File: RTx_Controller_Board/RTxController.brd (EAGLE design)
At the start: 161.3 x 90.2 mm, 197 parts, among them IC2 MAX5984C, J22 Debug Header, SW1 COM08720, U1 STM32F407ZXT, U2 TPD4S012, U3 KSZ8081, X4 MINI-USB-32005-301, X8 0826-1X1T-GJ-F

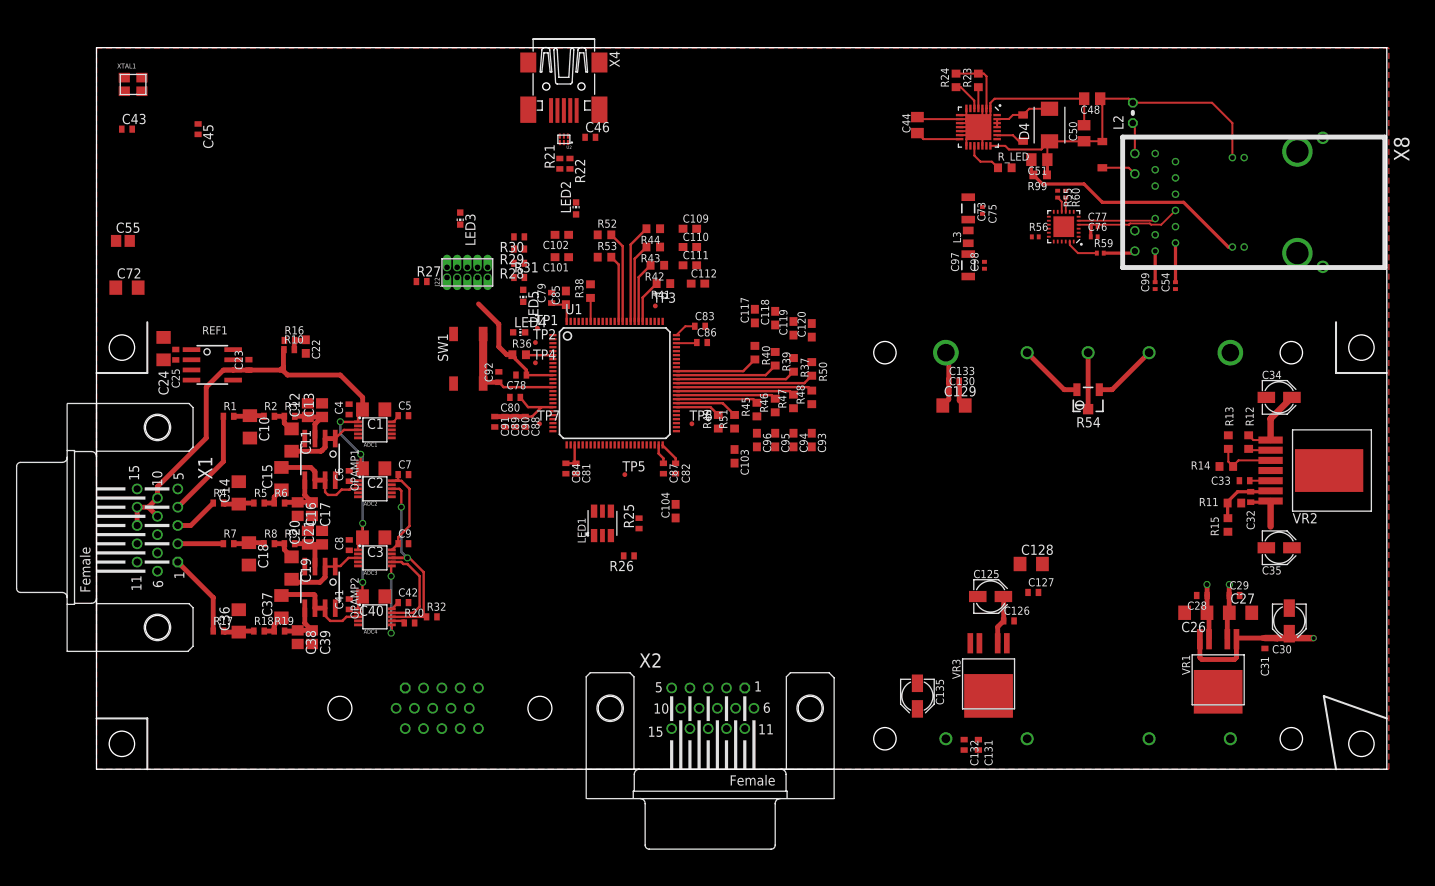
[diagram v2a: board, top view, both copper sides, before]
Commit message: Rtx Controller board updated, all that remains are power planes and rework by Rob. Initial check in of crystal.lbr.
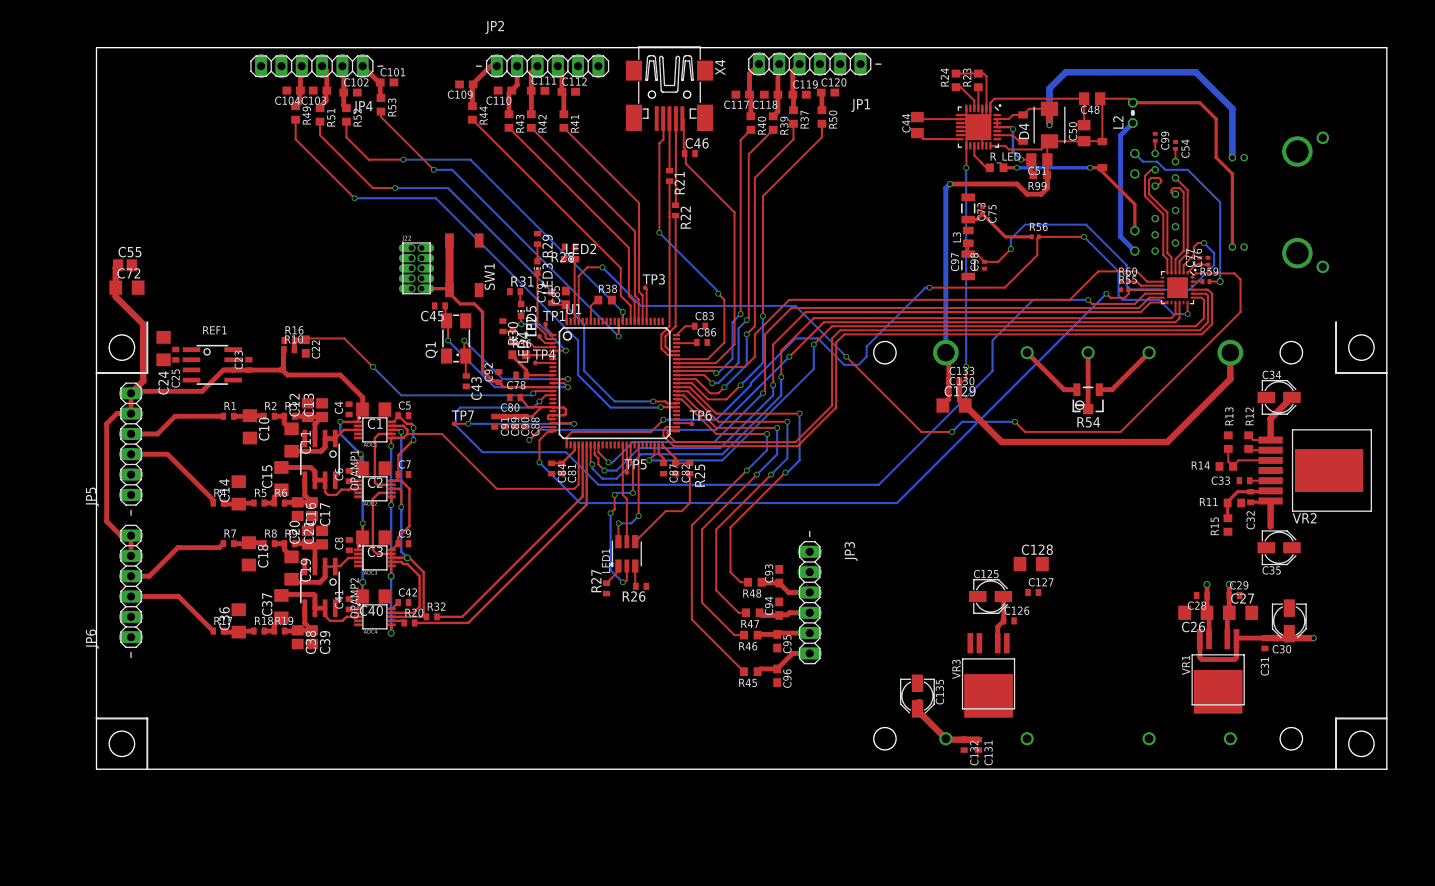
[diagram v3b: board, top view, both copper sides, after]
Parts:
- removed U2: TPD4S012, rtx:TPD4S012
- removed X1, X2, X3: (no value), con-subd:HDF15H
- removed XTAL1: ABM8G, motorFeedback:ABM8G
- added JP1, JP2, JP3, JP4, JP5, JP6: (no value), pinhead:1X06
- added Q1: (no value), crystal:CTS406
- moved C104 71.0 mm to (24.6, 84.8), turned to 180 degrees
- moved C103 69.1 mm to (27.9, 84.8), turned to 180 degrees
- moved R49 65.4 mm to (24.9, 82.0), turned to 270 degrees
- moved R51 64.5 mm to (27.9, 81.8), turned to 270 degrees
- moved C43 52.8 mm to (46.2, 48.5), turned to 270 degrees
- moved R27 44.8 mm to (63.8, 22.6), turned to 90 degrees
- moved C45 37.4 mm to (42.9, 57.9), turned to 180 degrees
- moved R52 35.6 mm to (31.2, 81.8), turned to 270 degrees
- moved R53 33.8 mm to (35.6, 83.1), turned to 270 degrees
- moved C109 33.3 mm to (46.2, 85.6), turned to 180 degrees
- moved R45 32.8 mm to (81.8, 12.2), turned to 180 degrees
- moved C102 31.8 mm to (31.8, 84.6), turned to 0 degrees
- moved R50 31.5 mm to (90.7, 81.5)
- moved R37 31.0 mm to (87.1, 81.5)
- moved C101 30.9 mm to (36.3, 85.9), turned to 0 degrees
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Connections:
- removed net SPI_NSS: ADC1.6, ADC1.9, ADC2.6, ADC3.6, ADC4.6
- net +5.000VREF: now also JP5.5, JP5.6, JP6.5, JP6.6; no longer X1.10, X1.13, X1.14, X1.9
- net ADC_CNV: now also ADC1.6, ADC1.9, ADC2.6, ADC3.6, ADC4.6
- net D+: no longer U2.1
- net D-: no longer U2.2
- net GND: now also JP1.1, JP1.2, JP2.5, JP2.6, JP3.1, JP3.2, JP4.5, JP4.6, JP5.1, JP5.2, JP6.1, JP6.2; no longer U2.4, X1.5, X1.6, X1.7, X1.8, X2.10, X2.5, X2.6, X2.7, X2.8, X3.10, X3.5, X3.6, X3.7, X3.8
- net N$14: now also JP6.4; no longer X1.2
- net N$42: now also JP3.6; no longer X2.15
- net N$45: now also JP3.5; no longer X2.14
- net N$46: now also JP3.4; no longer X2.13
- net N$47: now also JP3.3; no longer X2.12
- net N$48: now also JP4.4; no longer X2.4
- net N$49: now also JP4.3; no longer X2.3
- net N$50: now also JP4.2; no longer X2.2
- net N$51: now also JP4.1; no longer X2.1
- net N$52: now also JP2.4; no longer X3.4
- net N$53: now also JP2.3; no longer X3.3
- net N$54: now also JP2.2; no longer X3.2
- net N$55: now also JP2.1; no longer X3.1
- net N$6: now also JP5.4; no longer X1.4
- net N$61: now also JP1.3; no longer X3.15
- net N$62: now also JP1.4; no longer X3.14
- net N$63: now also JP1.5; no longer X3.13
- net N$64: now also JP1.6; no longer X3.12
- net N$7: now also JP6.3; no longer X1.1
- net N$9: now also JP5.3; no longer X1.3
- net OSC_IN: now also Q1.1; no longer XTAL1.1
- net OSC_OUT: now also Q1.3; no longer XTAL1.3
- net REF_MONITOR: now also U1.15; no longer U1.37
- net USB_ID: no longer U2.3
- net USB_VBUS: no longer U2.6
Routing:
- net ETH_MDC: track 0.00 -> 118.6 mm, vias 0 -> 2
- net EPHY_NRST: track 0.00 -> 115.3 mm, vias 0 -> 4
- net ETH_MDINT: track 0.00 -> 101.1 mm, vias 0 -> 4
- net ETH_MDIO: track 1.99 -> 96.8 mm, vias 0 -> 2
- net ETH_RMII_REF_CLK: track 0.00 -> 93.2 mm, vias 0 -> 2
- net ETH_CRS_DV: track 0.00 -> 89.7 mm, vias 0 -> 2
- net ETH_TXD1: track 0.00 -> 89.2 mm
- net ETH_RXD0: track 0.00 -> 86.5 mm, vias 0 -> 2
- net ETH_TXD0: track 0.00 -> 85.9 mm
- net ETH_RXD1: track 0.00 -> 84.7 mm, vias 0 -> 2
- net ETH_TX_EN: track 0.00 -> 84.5 mm, vias 0 -> 2
- net POE-: track 65.8 -> 137.7 mm, vias 0 -> 2
- net MCO1-ETH-CLK: track 0.00 -> 67.9 mm
- net ADC_CNV: track 0.00 -> 62.2 mm, vias 0 -> 4
- net WATCHDOG_LAT_OUT: track 5.64 -> 66.5 mm, vias 0 -> 2
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- removed copper zone on layer 1, net GND

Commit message: Repositioned LDO's created power planes.
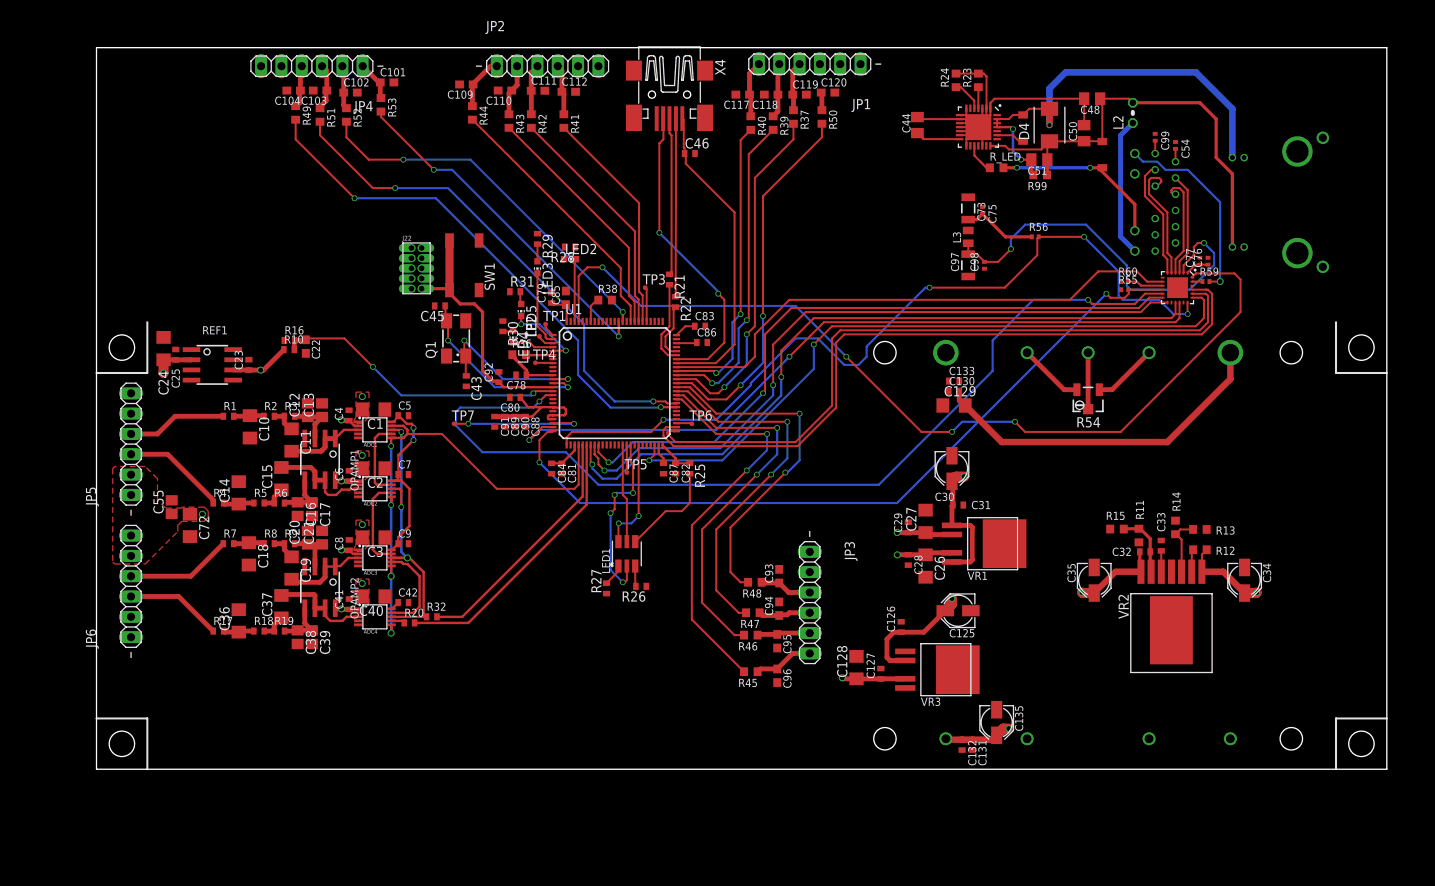
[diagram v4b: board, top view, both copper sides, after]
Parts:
- moved C30 46.3 mm to (106.9, 37.6)
- moved C31 42.1 mm to (107.7, 33.0), turned to 0 degrees
- moved C29 41.6 mm to (101.5, 30.2), turned to 90 degrees
- moved C27 41.0 mm to (103.6, 31.0), turned to 90 degrees
- moved C28 37.0 mm to (101.5, 26.2), turned to 270 degrees
- moved C26 34.3 mm to (103.6, 25.4), turned to 270 degrees
- moved VR1 32.9 mm to (112.0, 28.2), turned to 270 degrees
- moved C55 30.8 mm to (9.40, 32.8), turned to 90 degrees
- moved C72 30.7 mm to (11.7, 30.5), turned to 270 degrees
- moved VR2 28.6 mm to (134.4, 17.0), turned to 180 degrees
- moved C128 25.4 mm to (95.0, 12.7), turned to 90 degrees
- moved C35 23.5 mm to (124.7, 23.6), turned to 270 degrees
- moved C34 23.3 mm to (143.5, 23.6), turned to 270 degrees
- moved C127 21.6 mm to (98.0, 11.9), turned to 90 degrees
- moved C32 14.9 mm to (131.1, 27.2), turned to 180 degrees
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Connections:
- removed net VIO: ADC1.10, ADC2.10, ADC3.10, C5.1, C7.1, C9.1
- removed net VIO@10: ADC4.10, C42.1
- net +3.3V: now also ADC1.10, ADC2.10, ADC3.10, ADC4.10, C42.1, C5.1, C7.1, C9.1
- net +5.000VREF: now also JP5.1, JP5.2; no longer JP5.5, JP5.6
- net GND: now also JP5.5, JP5.6; no longer JP5.1, JP5.2
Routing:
- net +5.000VREF: track 112.6 -> 7.51 mm, vias 4 -> 6
- net POE+: track 99.9 -> 56.8 mm, vias 1 -> 0
- net POE-: track 137.7 -> 106.1 mm, vias 2 -> 0
- net +3.3V: track 55.5 -> 79.3 mm, vias 1 -> 3
- net VIO: track 22.7 -> 0.00 mm, vias 2 -> 0
- net D-: track 6.51 -> 19.7 mm
- net +8V: track 0.00 -> 13.1 mm, vias 0 -> 2
- net USB_D-: track 23.6 -> 10.6 mm
- net USB_D+: track 18.5 -> 7.07 mm
- net D+: track 10.8 -> 22.3 mm
- net +5V: track 7.19 -> 18.0 mm, vias 1 -> 5
- net +12V: track 33.2 -> 43.4 mm, vias 1 -> 3
- net VIO@10: track 1.13 -> 0.00 mm
- net +9-36V: track 20.4 -> 19.5 mm, vias 0 -> 2
- added copper zone on layer 3, net +12V
- added copper zone on layer 3, net +3.3V
- added copper zone on layer 1, net +5.000VREF
- added copper zone on layer 3, net +5.000VREF
- added copper zone on layer 3, net +5V
- added copper zone on layer 3, net +8V
- added copper zone on layer 3, net +9-36V
- added copper zone on layer 3, net POE+
- added copper zone on layer 3, net POE-

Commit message: Added termination resistors to RMII bus, adjusted width of digital signals.
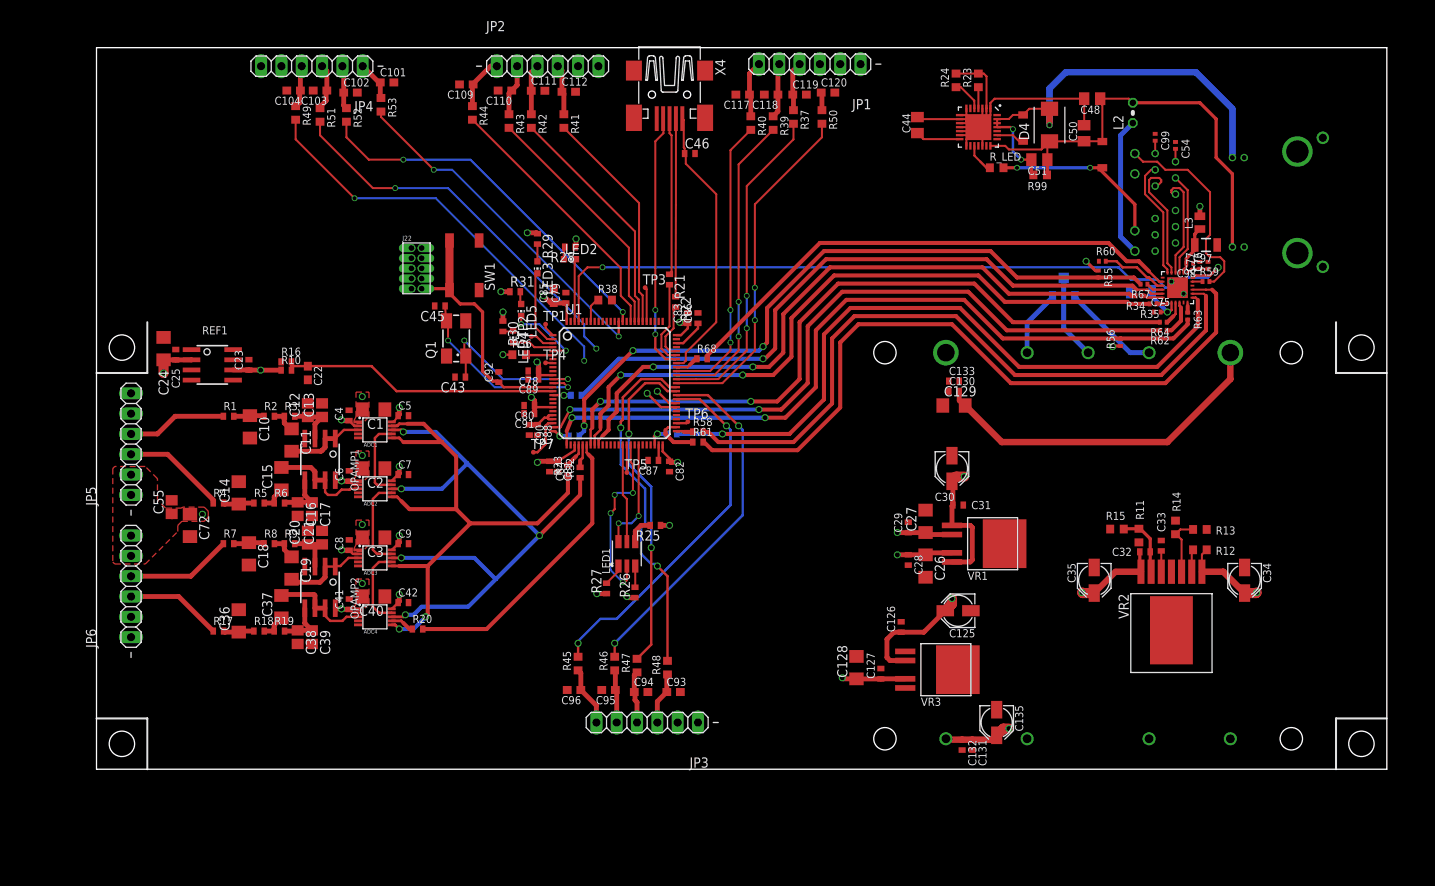
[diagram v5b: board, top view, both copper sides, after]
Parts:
- added R33, R57, R58, R61, R65, R66, R68: 33, motorFeedback:R0402
- added R34, R35, R62, R63, R64, R67: 33, rcl_custom:0402-C-NOSILK
- moved C97 29.8 mm to (138.7, 65.5), turned to 180 degrees
- moved L3 29.0 mm to (137.9, 68.3)
- moved R32 25.9 mm to (60.5, 37.1), turned to 90 degrees
- moved C98 25.7 mm to (136.7, 63.2), turned to 180 degrees
- moved C96 25.5 mm to (59.7, 9.91), turned to 180 degrees
- moved C75 25.3 mm to (132.6, 57.1), turned to 0 degrees
- moved JP3 25.2 mm to (68.8, 5.84), turned to 180 degrees
- moved C73 24.0 mm to (130.6, 59.7), flipped to the bottom, turned to 180 degrees
- moved C95 21.9 mm to (64.0, 9.91), turned to 180 degrees
- moved R45 21.6 mm to (60.2, 13.2), turned to 90 degrees
- moved C94 20.2 mm to (68.1, 9.65), turned to 0 degrees
- moved C93 19.6 mm to (72.1, 9.65), turned to 0 degrees
- moved R46 17.4 mm to (64.8, 13.2), turned to 90 degrees
- moved R56 17.0 mm to (128.0, 53.3), turned to 90 degrees
- moved R47 15.9 mm to (67.6, 13.0), turned to 90 degrees
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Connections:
- net N$72 renamed SPI_SCK_MCU
- new net N$72: R35.1, U3.13
- new net N$73: R33.2, U1.29
- new net N$74: R34.1, U3.12
- new net N$75: R57.1, U1.48
- new net N$76: R61.1, U1.52
- new net N$77: R58.1, U1.51
- new net N$78: R62.1, U3.16
- new net N$81: R65.1, U1.16
- new net N$83: R63.1, U3.18
- new net N$84: R64.1, U3.15
- new net N$85: R66.1, U1.25
- new net N$86: R68.1, U1.67
- new net N$87: R67.1, U3.10
- net ADC_CNV: now also R33.1; no longer U1.29
- net ETH_CRS_DV: now also R64.2; no longer U3.15
- net ETH_MDC: now also R65.2; no longer U1.16
- net ETH_MDINT: now also R63.2; no longer U3.18
- net ETH_MDIO: now also R66.2, R67.2; no longer U1.25, U3.10
- net ETH_RMII_REF_CLK: now also R62.2; no longer U3.16
- net ETH_RXD0: now also R35.2; no longer U3.13
- net ETH_RXD1: now also R34.2; no longer U3.12
- net ETH_TXD0: now also R58.2; no longer U1.51
- net ETH_TXD1: now also R61.2; no longer U1.52
- net ETH_TX_EN: now also R57.2; no longer U1.48
- net MCO1-ETH-CLK: now also R68.2; no longer U1.67
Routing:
- net VDDA_3.3: track 49.8 -> 6.31 mm, vias 2 -> 0
- net SPI_SCK: track 37.5 -> 80.8 mm, vias 3 -> 5
- net ETH_MDC: track 118.6 -> 84.3 mm, vias 2 -> 1
- net SPI_SCK_MCU: track 30.9 -> 2.94 mm
- net EPHY_NRST: track 115.3 -> 91.9 mm, vias 4 -> 2
- net +3.3V: track 79.3 -> 66.7 mm, vias 3 -> 23
- net N$44: track 17.7 -> 5.29 mm, vias 2 -> 0
- net ADC_CNV: track 62.2 -> 73.7 mm, vias 4 -> 2
- net ETH_MDIO: track 96.8 -> 86.3 mm, vias 2 -> 3
- net N$31: track 12.5 -> 3.46 mm
- net ETH_MDINT: track 101.1 -> 94.2 mm, vias 4 -> 2
- net USB_ID: track 38.4 -> 32.4 mm
- net N$76: track 0.00 -> 5.85 mm
- net N$78: track 0.00 -> 4.63 mm
- net USB_VBUS: track 39.2 -> 34.9 mm
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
